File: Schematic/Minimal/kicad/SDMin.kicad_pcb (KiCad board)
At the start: 2 copper layers, 88 x 91.2 mm, 83 parts, among them CON1 uSD_Card, P1 USB_B, P2 CONN_01X04, P3 CONN_01X04, P4 CONN_01X04, SW1 SW_PUSH, SW2 SW_PUSH, SW3 SW_PUSH, SW4 SW_PUSH, SW5 Switch_SPDT_x2, SW6 SW_PUSH, SW7 SW_PUSH, SW8 SW_PUSH, SW9 SW_PUSH, U1 PAM2301, U10 ADMP401-BB, U11 RN-52, U12 STA013, U2 XC9140, U3 MCP73811/2, U4 STM32L476R, U5 Lightware_SF10/A, U6 UART, U7 DebugPins, U8 MLX90393, U9 LS20031, X1 14.7456MHz

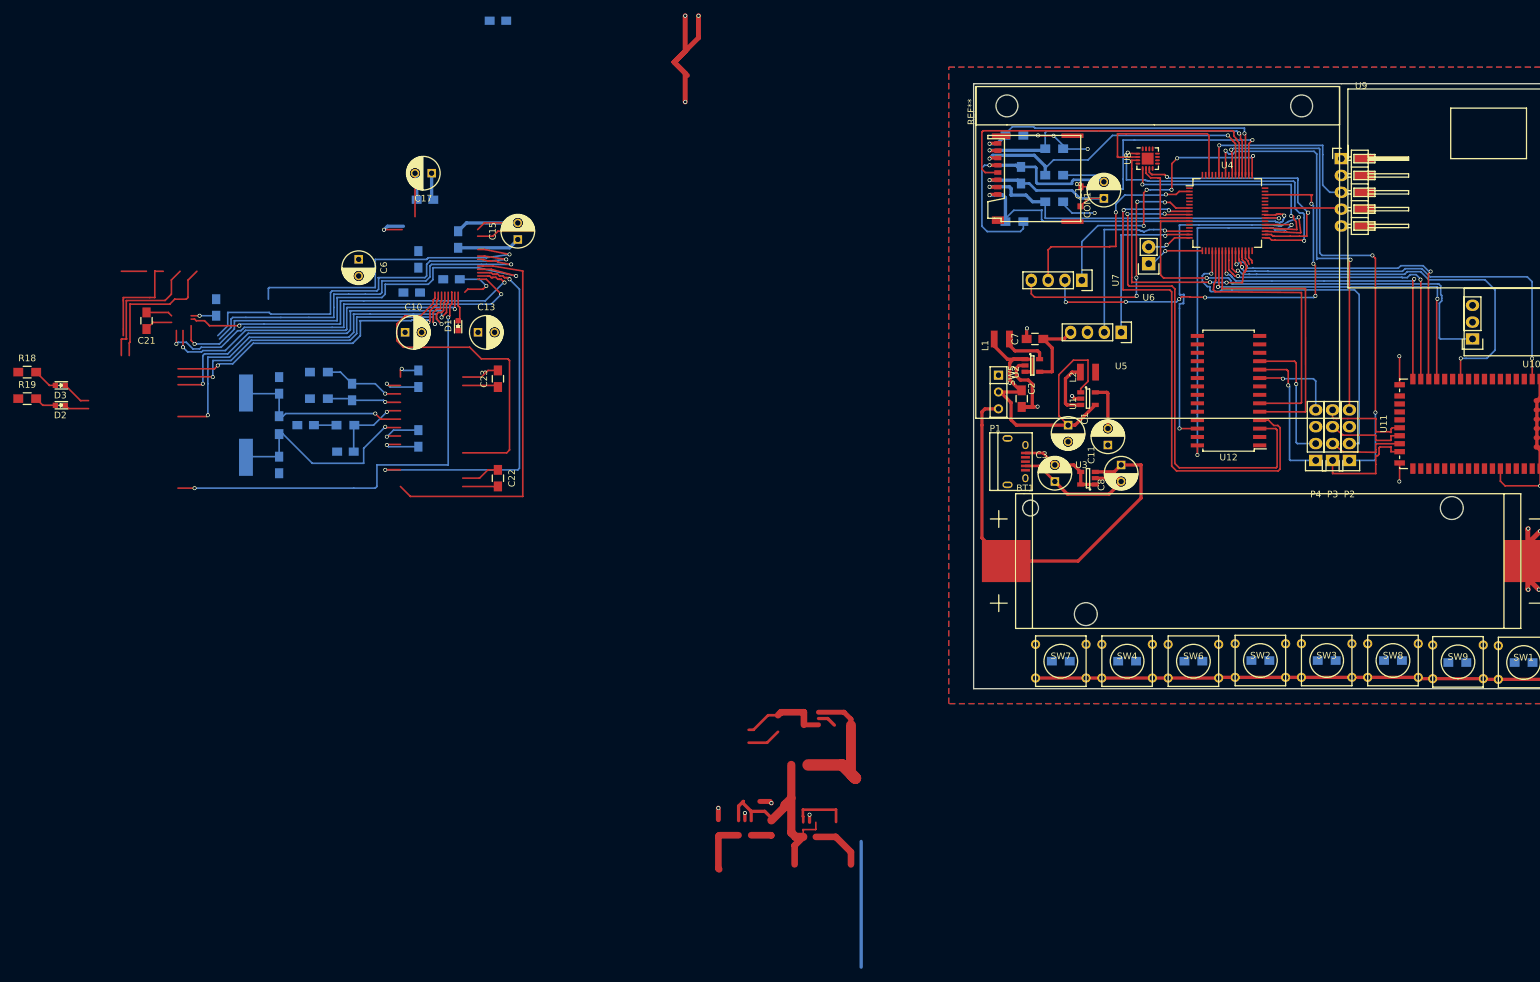
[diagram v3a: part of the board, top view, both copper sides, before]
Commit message: Progressing on the PCB. Completed pinout for the standard board.
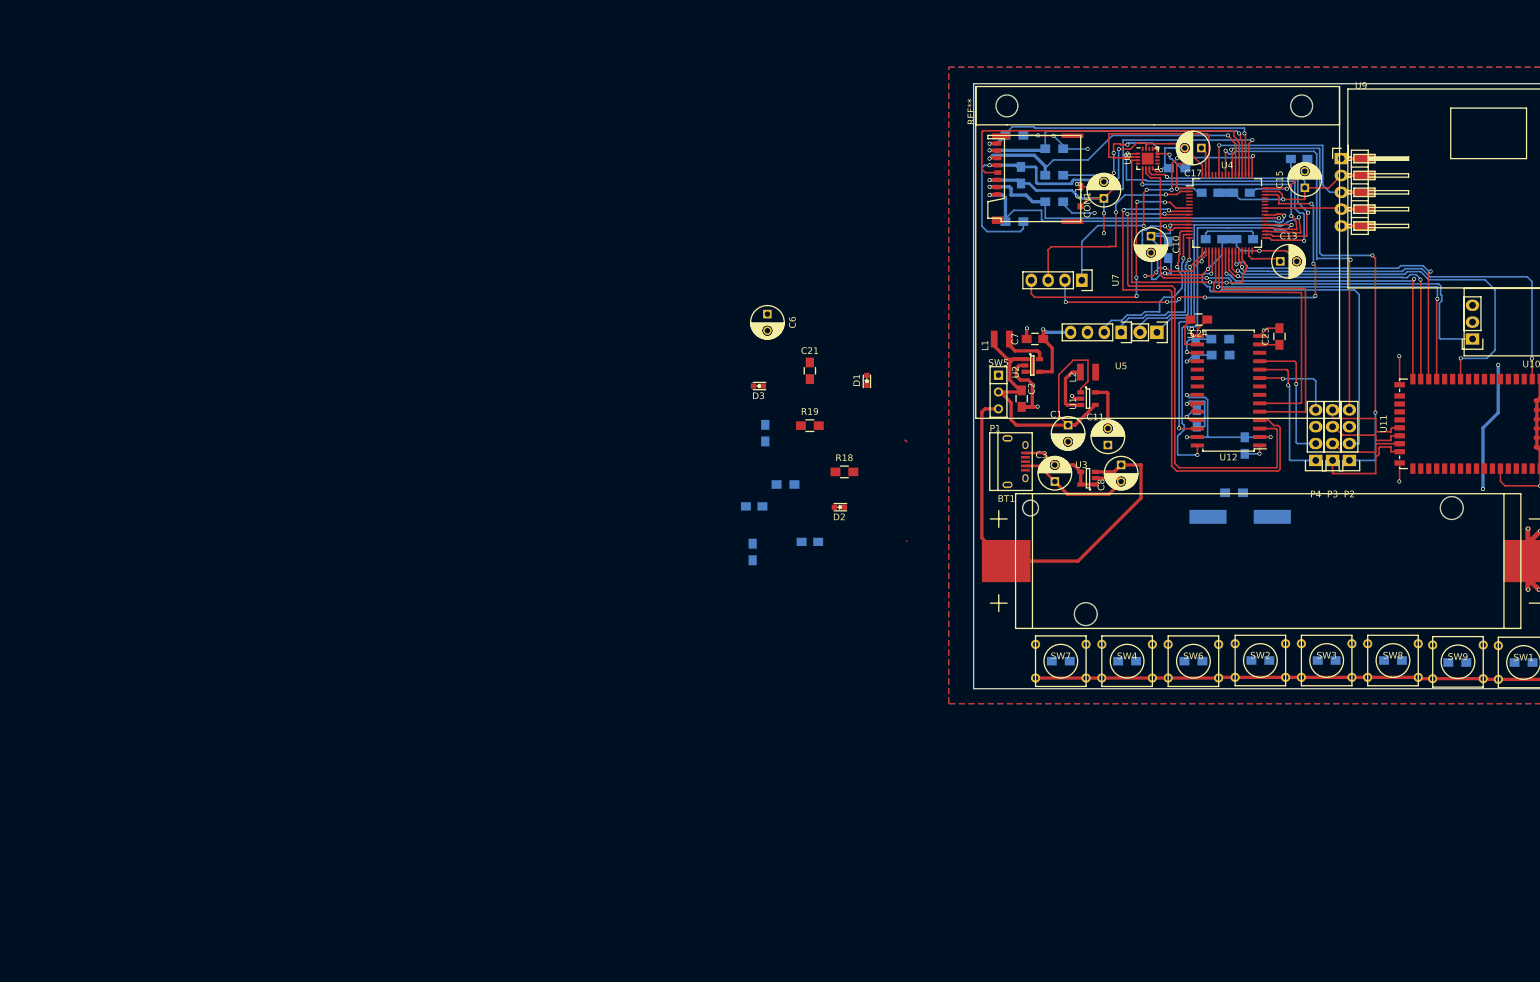
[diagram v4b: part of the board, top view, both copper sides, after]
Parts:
- C22: moved to B.Cu
- C24: moved to F.Cu
- moved X1 150.6 mm to (210.9, 136.8), turned to 180 degrees
- moved C20 146.5 mm to (201.4, 84.2), turned to 180 degrees
- moved R17 144.4 mm to (210.0, 133.2), turned to 0 degrees
- moved R15 136.2 mm to (208.0, 112.4), turned to 180 degrees
- moved R14 136.0 mm to (207.9, 110.0), turned to 180 degrees
- moved C14 127.4 mm to (219.8, 82.8), turned to 0 degrees
- moved C26 127.4 mm to (204.2, 111.3)
- moved R18 124.2 mm to (151.2, 130.1)
- moved C16 123.2 mm to (211.2, 88.0), turned to 0 degrees
- moved C13 121.5 mm to (217.0, 98.3)
- moved C9 121.3 mm to (207.0, 95.0)
- moved C12 119.8 mm to (211.7, 95.0), turned to 180 degrees
- moved C15 119.0 mm to (220.7, 87.2)
- moved D2 118.5 mm to (150.5, 135.4)
- moved R19 118.1 mm to (146.1, 123.1)
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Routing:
- net (no net): track 1099.7 -> 20.2 mm, vias 31 -> 2
- net GND: track 166.1 -> 279.2 mm, vias 15 -> 30
- net +3V3: track 215.3 -> 291.2 mm, vias 10 -> 15
- net Net-(C30-Pad1): track 32.2 -> 0.00 mm, vias 1 -> 0
- net Net-(C29-Pad1): track 27.3 -> 0.00 mm, vias 1 -> 0
- net PA2_UART: track 6.71 -> 20.9 mm
- net Net-(C27-Pad1): track 11.9 -> 0.00 mm, vias 1 -> 0
- net PA3_UART: track 8.91 -> 17.3 mm
- net Net-(D1-Pad2): track 6.73 -> 0.35 mm
- net PC6_MP3-DR: track 54.4 -> 60.0 mm
- net Net-(C26-Pad1): track 11.2 -> 5.77 mm
- net Net-(C26-Pad2): track 12.3 -> 7.03 mm
- net Net-(D3-Pad1): track 4.45 -> 0.00 mm
- net PB9_MAG-CS: track 26.5 -> 30.4 mm
- net Net-(D3-Pad2): track 3.73 -> 0.00 mm
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
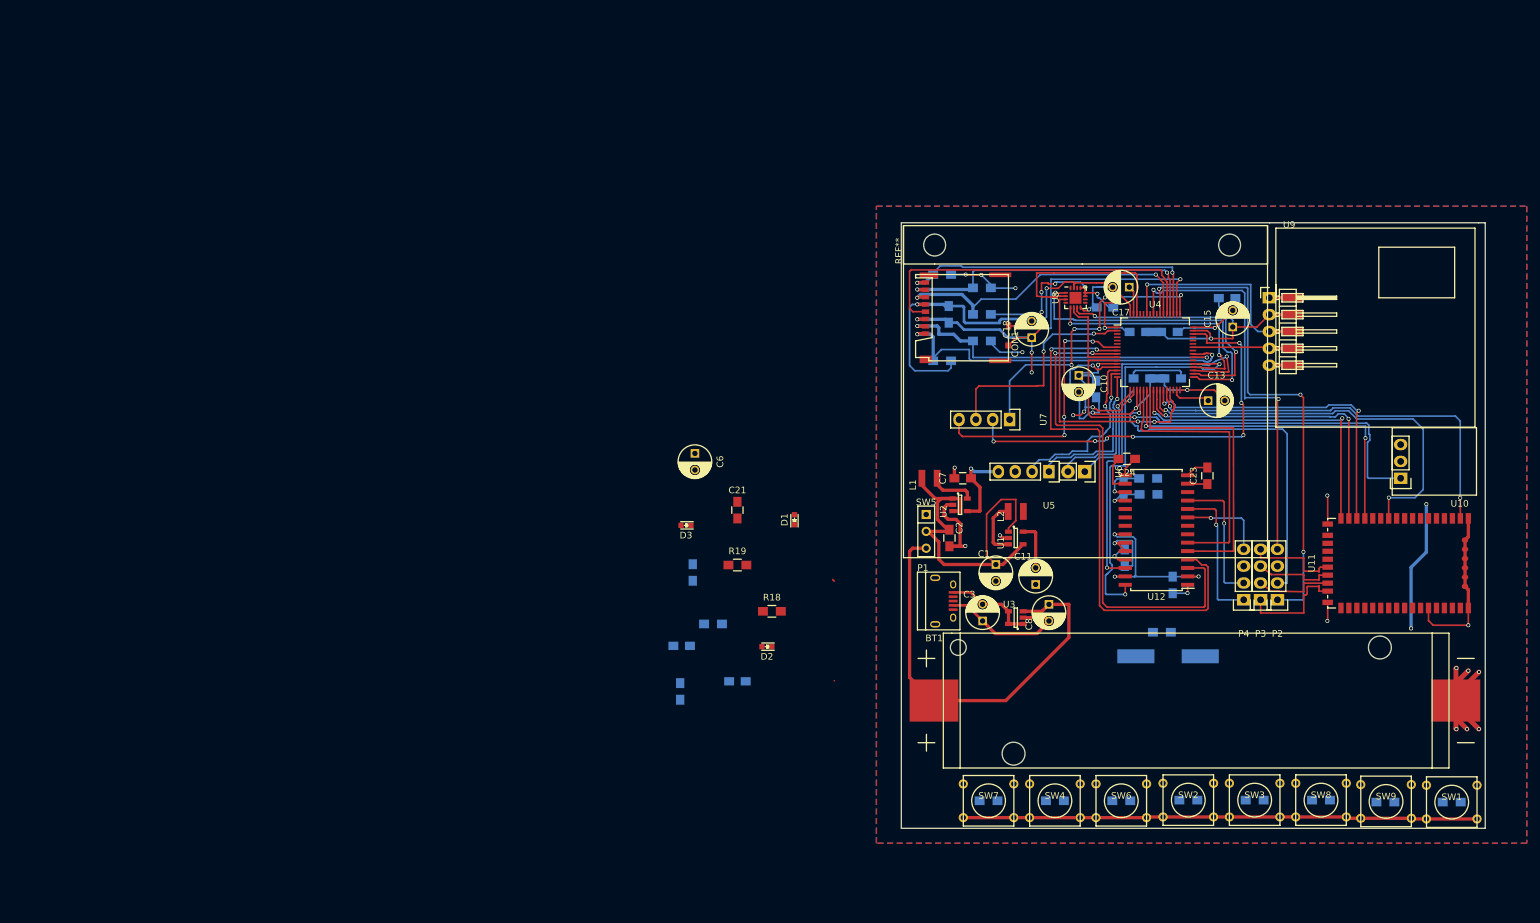
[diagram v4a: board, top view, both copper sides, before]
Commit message: Working on PCB#4, now with FreeRouting
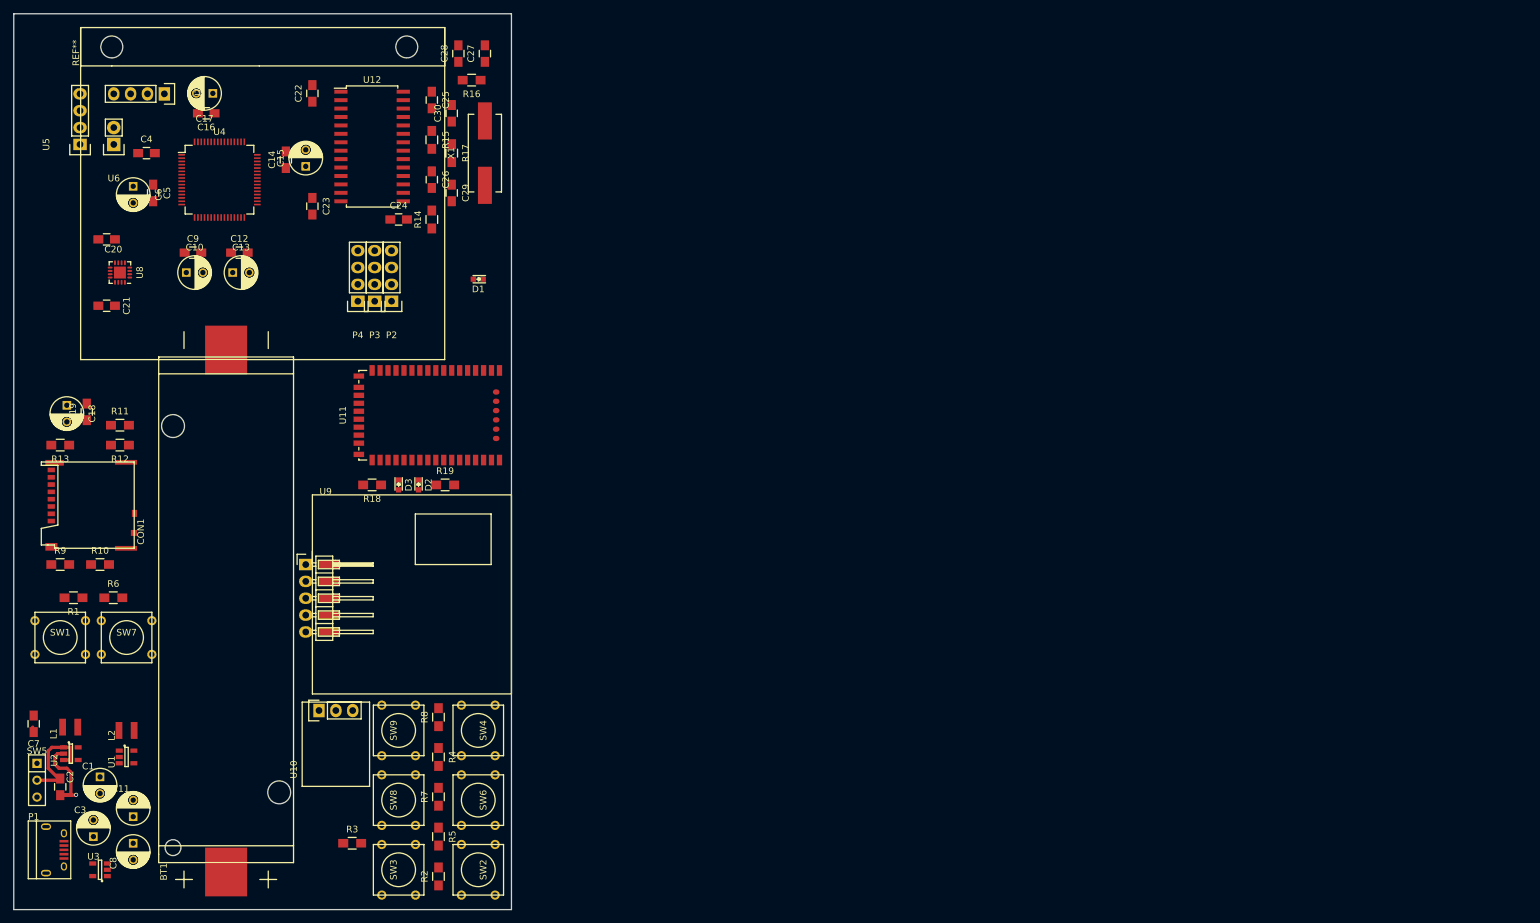
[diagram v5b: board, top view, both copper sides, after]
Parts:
- C12, C14, C16, C19, C20, C22, C25, C26, C27, C28, C29, C30, C4, C5, C9, R1, R10, R11, R12, R13, R14, R15, R16, R17, R2, R3, R4, R5, R6, R7, R8, R9, X1: moved to F.Cu
- moved SW1 211.2 mm to (44.0, 134.0)
- moved R1 210.0 mm to (46.0, 128.0), turned to 180 degrees
- moved U10 166.7 mm to (83.0, 145.0), turned to 90 degrees
- moved U6 154.4 mm to (52.1, 59.7), turned to 180 degrees
- moved U5 154.1 mm to (47.0, 59.7), turned to 90 degrees
- moved C4 151.8 mm to (57.0, 61.0), turned to 0 degrees
- moved C20 150.8 mm to (51.0, 74.0), turned to 0 degrees
- moved U9 150.7 mm to (81.0, 123.0)
- moved C22 149.3 mm to (82.0, 52.0), turned to 90 degrees
- moved SW9 149.2 mm to (95.0, 148.0), turned to 90 degrees
- moved C16 148.8 mm to (66.0, 55.0), turned to 180 degrees
- moved C13 148.3 mm to (70.0, 79.0)
- moved U11 147.7 mm to (102.0, 100.5)
- moved C18 145.8 mm to (45.0, 99.0), turned to 270 degrees
- moved C5 145.1 mm to (58.0, 67.0)
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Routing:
- net +3V3: track 291.2 -> 0.00 mm, vias 15 -> 0
- net GND: track 279.2 -> 14.3 mm, vias 30 -> 1
- net PC0_MP3-SCL: track 82.5 -> 0.00 mm, vias 2 -> 0
- net PC1_MP3-SDA: track 77.8 -> 0.00 mm, vias 2 -> 0
- net PB3_BTpcm-CLK: track 76.2 -> 0.00 mm, vias 3 -> 0
- net PC3_mic: track 68.7 -> 0.00 mm, vias 1 -> 0
- net PA13_dbg: track 63.9 -> 0.00 mm, vias 7 -> 0
- net Net-(BT1-Pad1): track 63.4 -> 0.00 mm
- net PB2_BT-GP2: track 62.6 -> 0.00 mm, vias 2 -> 0
- net PB0_BT-GP9: track 62.2 -> 0.00 mm, vias 2 -> 0
- net PB5_BTpcm-IN: track 61.9 -> 0.00 mm, vias 2 -> 0
- net PC6_MP3-DR: track 60.0 -> 0.00 mm, vias 2 -> 0
- net PB14_MP3-RST: track 59.6 -> 0.00 mm, vias 2 -> 0
- net PC9_SD-D1: track 56.2 -> 0.00 mm, vias 2 -> 0
- net PA4_BTpcm-Sync: track 54.8 -> 0.00 mm, vias 1 -> 0
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- removed copper zone on F.Cu, net +3V3
- removed copper zone on B.Cu, net GND
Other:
- board size 88 x 91.2 mm -> 75 x 135 mm
